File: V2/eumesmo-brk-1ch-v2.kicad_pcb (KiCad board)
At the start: 2 copper layers, 22 x 28 mm, 3 parts, among them J1 RJ45, J2 1x4P 5,08 SCREW

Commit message: V2.0.0 created
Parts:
- J2: value 1x4P 5,08 SCREW -> 250-204; footprint Tales:TerminalBlock_Dibo_DB128L-5.08-4P_1x04_P5.08mm_Horizontal -> Tales:TerminalBlock_Wago_250-204_1x04_P3.5mm_45Degree
- moved J2 4.07 mm to (141.8, 110.0)
- moved J1 3.00 mm to (141.0, 98.0)
- moved G*** 1.00 mm to (148.5, 101.0)
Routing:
- net /+24V: track 18.6 -> 13.8 mm
- net /SW2: track 17.8 -> 14.3 mm
- net /SW1: track 29.8 -> 30.6 mm
- net /SW3: track 18.2 -> 19.0 mm
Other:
- board size 22 x 28 mm -> 22 x 32 mm
- board text added: "eumesmo-brk-1ch-v2"
- board text removed: "eumesmo-brk-1ch-v1"

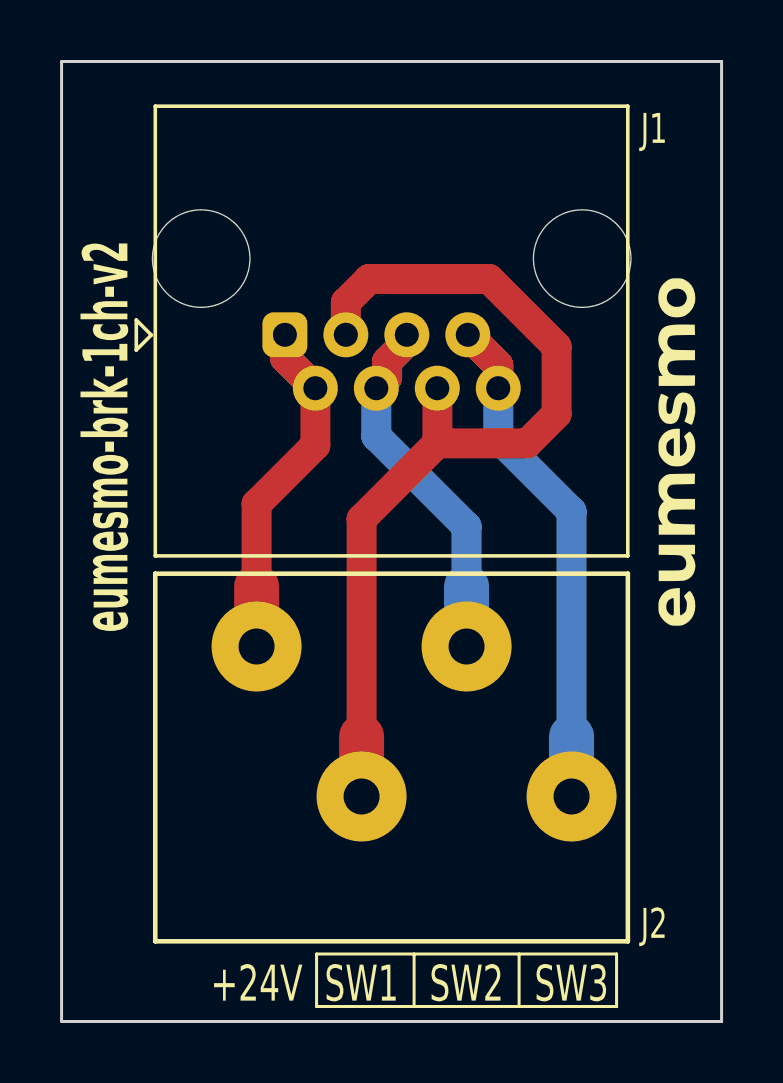
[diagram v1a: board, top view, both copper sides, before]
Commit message: Added revision date to silkscreen.
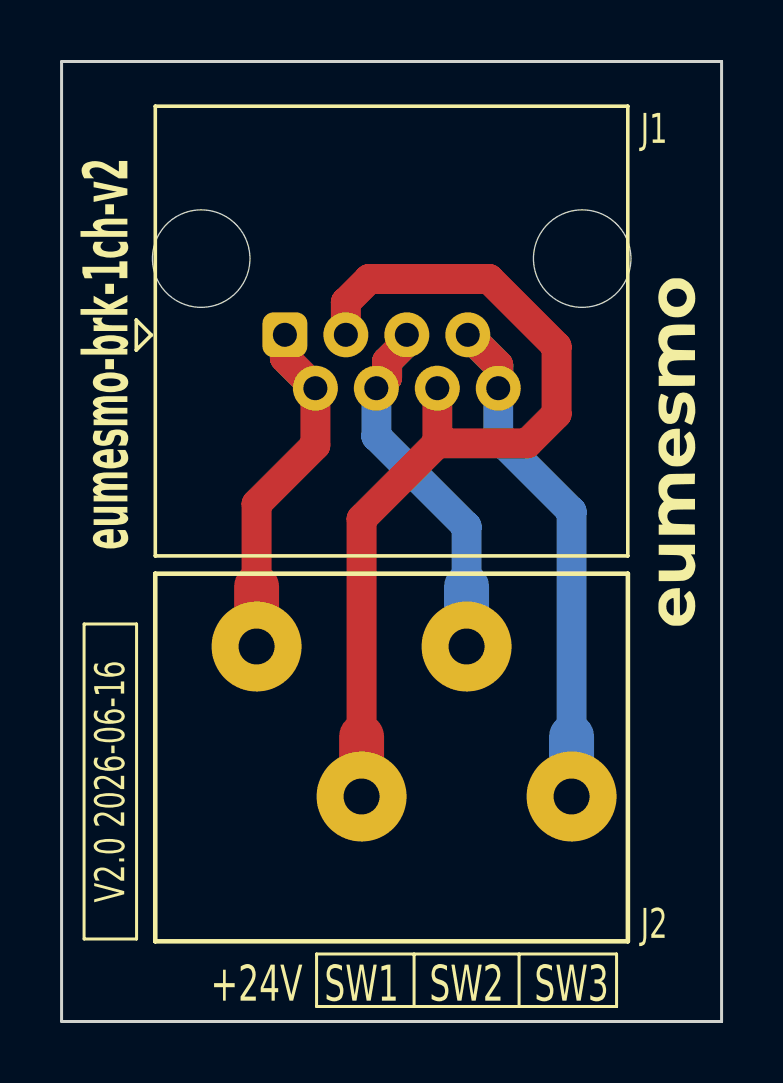
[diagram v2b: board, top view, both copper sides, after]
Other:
- board text added: "V2.0 2026-06-16"
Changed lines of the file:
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@@
+	)
+	(gr_rect
+		(start 130.75 106.75)
+		(end 132.5 117.25)
+		(stroke
+			(width 0.1)
+			(type default)
+		)
+		(fill no)
+		(layer "F.SilkS")
 	)
 	(gr_rect
@@
 		(fill no)
 		(layer "Edge.Cuts")
+	)
+	(gr_text "V2.0 2026-06-16"
+		(at 131.625 112 90)
+		(layer "F.SilkS")
+		(effects
+			(font
+				(size 1 0.7)
+				(thickness 0.1)
+			)
+		)
 	)
 	(gr_text "+24V"
@@
 	)
 	(gr_text "eumesmo-brk-1ch-v2"
-		(at 131.5 100.5 90)
+		(at 131.5 97.75 90)
 		(layer "F.SilkS")
 		(effects

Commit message: Release V2.0.0
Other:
- board text added: "V2.0 2026-06-17"
- board text removed: "V2.0 2026-06-16"
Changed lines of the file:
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@@
 	(title_block
 		(title "eumesmo 1 Channel RJ45 Breakout Board")
-		(date "2026-06-14")
+		(date "2026-06-17")
 		(rev "V2.0")
 	)
@@
 		(layer "Edge.Cuts")
 	)
-	(gr_text "V2.0 2026-06-16"
+	(gr_text "V2.0 2026-06-17"
 		(at 131.625 112 90)
 		(layer "F.SilkS")
